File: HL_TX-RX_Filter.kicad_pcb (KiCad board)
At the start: 2 copper layers, 100 x 100 mm, 194 parts, among them J1 To Antenna, J10 CNR4, J2 From Tx, J3 ICSP, J4 Input1, J5 SCL SDA, J6 To Rx in, J7 CNR1, J8 CNR3, J9 CNR2, Q1 2N7002, Q2 2N7002, Q3 2N7002, Q4 2N7002, Q5 2N7002, Q6 2N7002, Q7 2N7002, Q8 2N7002, U1 LD1117S33TR, U10 PE4259, U11 PE4259, U12 PE4259, U13 PE4259, U2 ATMEGA328-AU, U3 PE4259, U4 PE4259, U5 PE4259, U6 PE4259, U7 PE4259, U8 PE4259, U9 PE4259

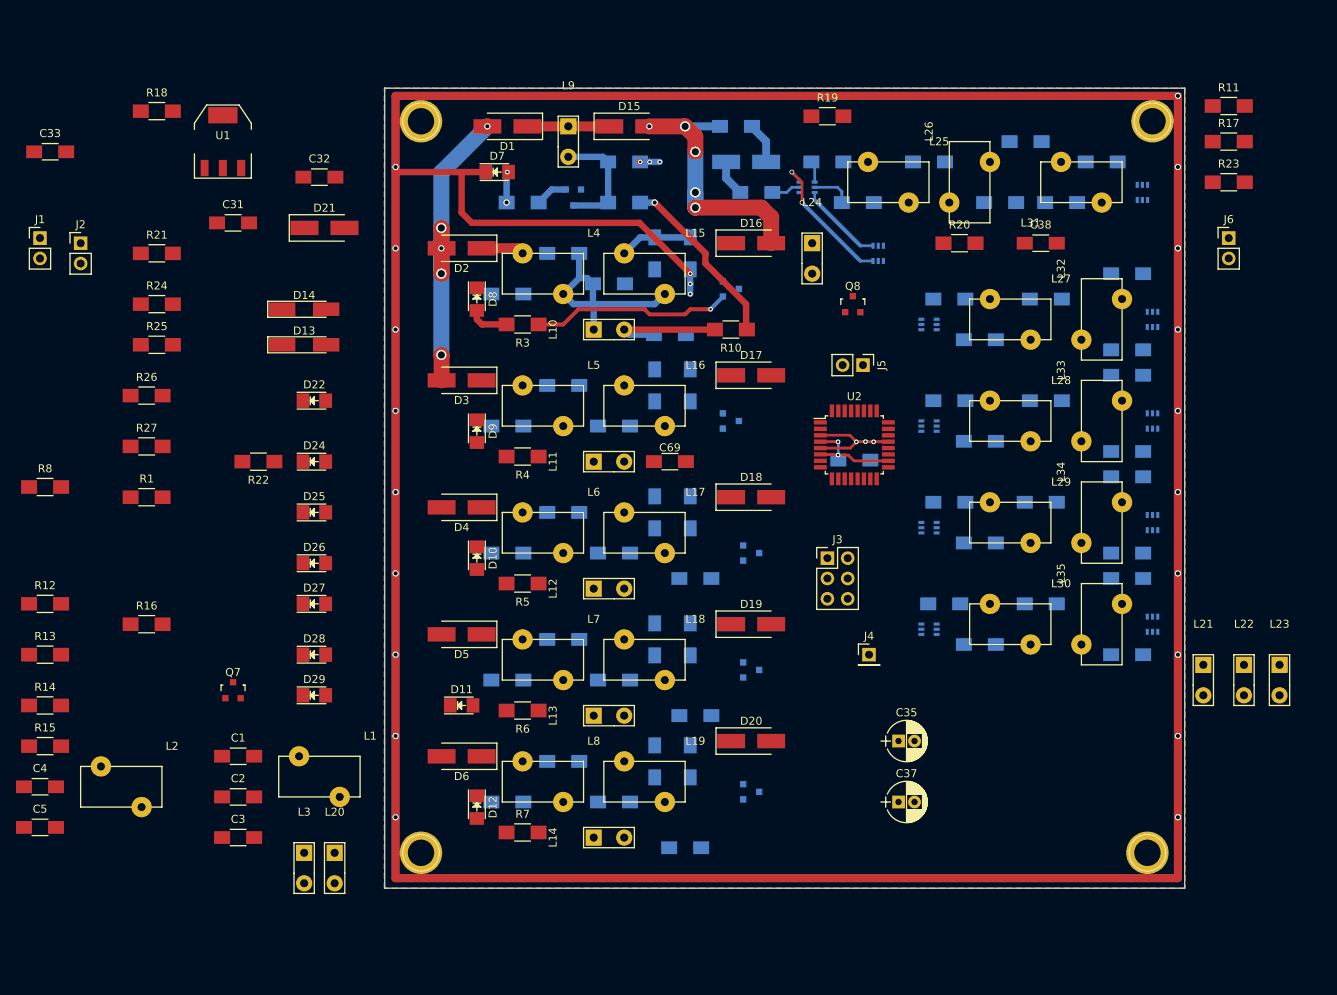
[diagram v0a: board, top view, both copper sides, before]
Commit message: Squeezed up Tx filters to hold 30M filter
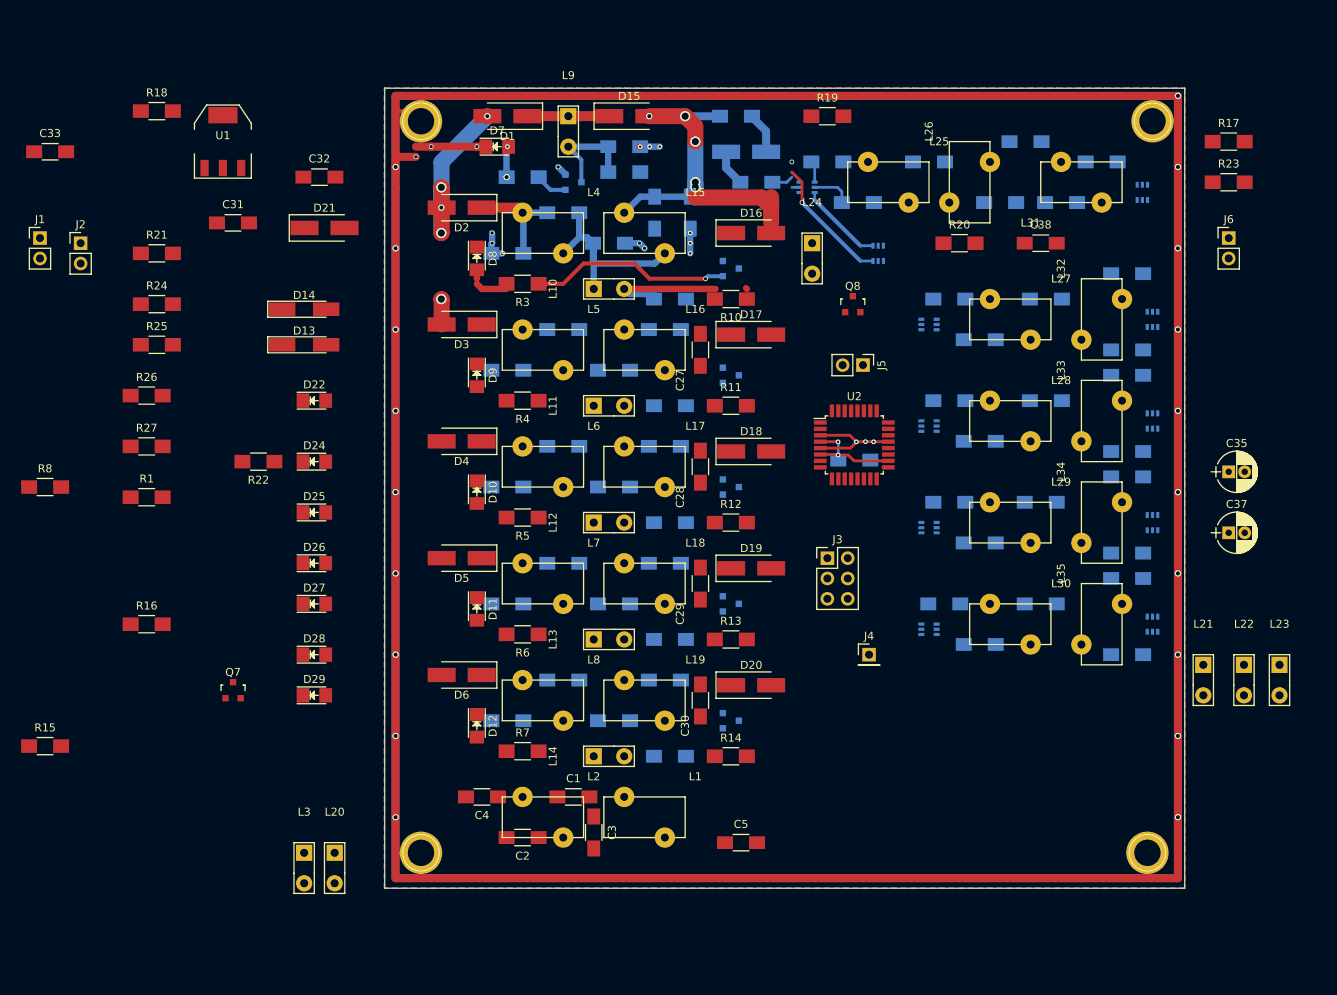
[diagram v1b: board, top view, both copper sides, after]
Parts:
- C27, C28, C29, C30: moved to F.Cu
- C69: moved to B.Cu
- moved C5 87.7 mm to (169.5, 154.3)
- moved R12 86.3 mm to (168.3, 114.3)
- moved R14 86.0 mm to (168.3, 143.5)
- moved R13 85.7 mm to (168.3, 128.9)
- moved R11 72.6 mm to (168.3, 99.7)
- moved C4 55.3 mm to (137.2, 148.6), turned to 180 degrees
- moved C37 53.3 mm to (230.5, 115.6)
- moved C35 53.3 mm to (230.5, 108.0)
- moved L2 52.8 mm to (139.7, 153.7)
- moved C3 44.5 mm to (151.1, 153.0), turned to 270 degrees
- moved C1 42.2 mm to (148.6, 148.6)
- moved L1 41.0 mm to (152.4, 153.7)
- moved C2 35.9 mm to (142.2, 153.7), turned to 180 degrees
- moved D11 12.2 mm to (136.5, 125.1), turned to 270 degrees
- moved C72 11.6 mm to (160.7, 143.5)
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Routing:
- net GND: track 859.2 -> 44.9 mm, vias 28 -> 17
- net (no net): track 0.00 -> 798.8 mm, vias 0 -> 21
- net Net-(C32-Pad1): track 34.6 -> 8.84 mm, vias 5 -> 1
- net Net-(C38-Pad1): track 22.5 -> 0.00 mm, vias 1 -> 0
- net Net-(C2-Pad1): track 43.8 -> 28.6 mm
- net Net-(C21-Pad2): track 9.08 -> 21.7 mm, vias 0 -> 4
- net Net-(C11-Pad1): track 5.38 -> 13.6 mm
- net Net-(C11-Pad2): track 27.4 -> 25.7 mm
- net Net-(C67-Pad1): track 14.9 -> 13.5 mm
- net 3V3: vias 4 -> 3

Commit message: Re-annotated board
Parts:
- removed U13: PE4259, TO_SOT_Packages_SMD:SC-70-6
- added R28: R, Resistors_SMD:R_1206_HandSoldering, F.Cu at (108.0, 121.9)
- added R29: R, Resistors_SMD:R_1206_HandSoldering, F.Cu at (101.0, 121.9)
- added R30: R, Resistors_SMD:R_1206_HandSoldering, F.Cu at (94.0, 121.9)
- added R31: R, Resistors_SMD:R_1206_HandSoldering, F.Cu at (108.0, 116.8)
- added R32: R, Resistors_SMD:R_1206_HandSoldering, F.Cu at (101.0, 116.8)
- added R33: R, Resistors_SMD:R_1206_HandSoldering, F.Cu at (94.0, 116.8)
- C1, C2, C3, C4, C5: moved to B.Cu
- C16: value 200p -> .1u
- C17: value 300p -> .1u
- C18: value 560p -> .1u
- C19: value 1082p -> .1u
- C20: value 2100p -> .1u
- C21: value 43p -> .1u
- C22: value 130p -> 300p
- C23: value 220p -> 560p
- C24: value 270p -> 1082p
- C25: value 552p -> 2100p
- C26: value 74p -> 200p
- C27: value 120p -> 43p
- C28: value 180p -> 130p
- C29: value 390p -> 220p
- C30: value 736p -> 270p
- C31: value 22p -> 552p
- C32: value C -> 74p
- C33: value 0.1u -> 120p
- C34: value 0.1 -> 180p
- C35: value 4.7u -> 390p; footprint Capacitors_THT:CP_Radial_D5.0mm_P2.00mm -> Capacitors_SMD:C_1206_HandSoldering
- C36: value C -> 736p
- C37: value 4.7u -> 22p; footprint Capacitors_THT:CP_Radial_D5.0mm_P2.00mm -> Capacitors_SMD:C_1206_HandSoldering
- C38: value 0.1u -> C
- C40: value 3000p -> 0.1
- C41: value 0.012u -> 4.7u; footprint Capacitors_SMD:C_1206_HandSoldering -> Capacitors_THT:CP_Radial_D5.0mm_P2.00mm
- C42: value 1600p -> C
- C43: value 1500p -> 4.7u; footprint Capacitors_SMD:C_1206_HandSoldering -> Capacitors_THT:CP_Radial_D5.0mm_P2.00mm
- C44: value 680p -> 0.1u
- C45: value 470p -> 0.1u
- C46: value 270p -> 3000p
- C47: value 2400p -> 0.012u
- C48: value 8200p -> 1600p
- C49: value 3900p -> 1500p
- C50: value 2400p -> 680p
- C51: value 1500p -> 470p
- C52: value 1800p -> 270p
- C53: value 680p -> 2400p
- C54: value 340p -> 8200p
- C55: value 236p -> 3900p
- C56: value 130p -> 2400p
- C57: value 3000p -> 1500p
- C58: value 2700p -> 1800p
- C59: value 1220p -> 680p
- C60: value 780p -> 340p
- C61: value 510p -> 236p
- C62: value 2400p -> 130p
- C63: value 2000p -> 3000p
- C64: value 1000p -> 2700p
- C65: value 680p -> 1220p
- C66: value 360p -> 780p
- C67: value .1u -> 510p
- C68: value .1u -> 2400p
- C69: value .1u -> 2000p
- C70: value .1u -> 1000p
- C71: value .1u -> 680p
- C72: value .1u -> 360p
- J1: value To Antenna -> CNR1; footprint Pin_Headers:Pin_Header_Straight_1x02_Pitch2.54mm -> Connectors:1pin
- J10: value CNR4 -> To Rx in; footprint Connectors:1pin -> Pin_Headers:Pin_Header_Straight_1x02_Pitch2.54mm
- J2: value From Tx -> CNR3; footprint Pin_Headers:Pin_Header_Straight_1x02_Pitch2.54mm -> Connectors:1pin
- J3: value ICSP -> CNR2; footprint Pin_Headers:Pin_Header_Straight_2x03_Pitch2.54mm -> Connectors:1pin
- J4: value Input1 -> CNR4; footprint Pin_Headers:Pin_Header_Straight_1x01_Pitch2.54mm -> Connectors:1pin
- J5: value SCL SDA -> To Antenna
- J6: value To Rx in -> From Tx
- J7: value CNR1 -> ICSP; footprint Connectors:1pin -> Pin_Headers:Pin_Header_Straight_2x03_Pitch2.54mm
- J8: value CNR3 -> SCL SDA; footprint Connectors:1pin -> Pin_Headers:Pin_Header_Straight_1x02_Pitch2.54mm
- J9: value CNR2 -> Input1; footprint Connectors:1pin -> Pin_Headers:Pin_Header_Straight_1x01_Pitch2.54mm
- R10, R9: value 100k -> R
- R11: value R -> 1k
- R12, R13: value R -> 100k
- R21: value 10k -> R
- R27: value R -> 10k
- R8: value 1k -> R
- U1: value LD1117S33TR -> ATMEGA328-AU; footprint TO_SOT_Packages_SMD:SOT-223 -> Housings_QFP:TQFP-32_7x7mm_Pitch0.8mm
- U10, U11, U12, U3, U4, U5, U6, U7, U8, U9: footprint TO_SOT_Packages_SMD:SC-70-6 -> TO_SOT_Packages_SMD:SOT-363_SC-70-6_Handsoldering
- U2: value ATMEGA328-AU -> PE4259; footprint Housings_QFP:TQFP-32_7x7mm_Pitch0.8mm -> TO_SOT_Packages_SMD:SOT-363_SC-70-6_Handsoldering
- moved L21 137.0 mm to (91.1, 146.1)
- moved L22 136.2 mm to (96.9, 145.4)
- moved L23 134.5 mm to (103.1, 146.3)
- moved J2 134.2 mm to (220.3, 64.1)
- moved R15 92.1 mm to (174.6, 141.0), turned to 270 degrees
- moved U1 87.5 mm to (183.5, 104.8)
- moved J8 81.7 mm to (194.9, 141.6)
- moved J7 78.1 mm to (185.4, 118.7)
- moved U2 66.1 mm to (175.0, 170.1)
- moved J4 60.4 mm to (130.2, 154.9)
- moved C41 60.3 mm to (184.8, 134.6)
- moved J9 59.5 mm to (83.8, 117.5)
- moved L20 57.6 mm to (175.9, 148.6)
- moved J5 57.1 mm to (170.2, 149.9), turned to 0 degrees
- moved J3 53.9 mm to (220.3, 154.9)
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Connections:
- C16 pad 1: Net-(C11-Pad2) -> Net-(C16-Pad1)
- C17 pad 1: Net-(C12-Pad2) -> Net-(C17-Pad1)
- C18 pad 1: Net-(C13-Pad2) -> Net-(C18-Pad1)
- C19 pad 1: Net-(C14-Pad2) -> Net-(C19-Pad1)
- C20 pad 1: Net-(C15-Pad2) -> Net-(C20-Pad1)
- C21 pad 1: Net-(C11-Pad2) -> Net-(C21-Pad1)
- C21 pad 2: Net-(C21-Pad2) -> GND
- C22 pad 2: Net-(C22-Pad2) -> GND
- C23 pad 2: Net-(C23-Pad2) -> GND
- C24 pad 2: Net-(C24-Pad2) -> GND
- C25 pad 2: Net-(C25-Pad2) -> GND
- C26 pad 1: Net-(C21-Pad2) -> Net-(C11-Pad2)
- C27 pad 1: Net-(C22-Pad2) -> Net-(C11-Pad2)
- C27 pad 2: GND -> Net-(C27-Pad2)
- C28 pad 1: Net-(C23-Pad2) -> Net-(C12-Pad2)
- C28 pad 2: GND -> Net-(C28-Pad2)
- C29 pad 1: Net-(C24-Pad2) -> Net-(C13-Pad2)
- C29 pad 2: GND -> Net-(C29-Pad2)
- C30 pad 1: Net-(C25-Pad2) -> Net-(C14-Pad2)
- C30 pad 2: GND -> Net-(C30-Pad2)
- C31 pad 1: Net-(C31-Pad1) -> Net-(C15-Pad2)
- C32 pad 1: Net-(C32-Pad1) -> Net-(C27-Pad2)
- C32 pad 2: Net-(C32-Pad2) -> GND
- C33 pad 1: Net-(C31-Pad2) -> Net-(C28-Pad2)
- C33 pad 2: Net-(C33-Pad2) -> GND
- C34 pad 1: 3V3 -> Net-(C29-Pad2)
- C35 pad 1: 3V3 -> Net-(C30-Pad2)
- C36 pad 1: Net-(C32-Pad1) -> Net-(C31-Pad2)
- C36 pad 2: Net-(C36-Pad2) -> GND
- C37 pad 1: 3V3 -> Net-(C37-Pad1)
- C37 pad 2: GND -> Net-(C37-Pad2)
- C38 pad 2: GND -> Net-(C38-Pad2)
- C39 pad 1: Net-(C39-Pad1) -> Net-(C37-Pad2)
- C40 pad 1: Net-(C40-Pad1) -> 3V3
- C40 pad 2: Net-(C40-Pad2) -> GND
- C41 pad 1: Net-(C41-Pad1) -> 3V3
- C42 pad 1: Net-(C40-Pad2) -> Net-(C38-Pad1)
- C43 pad 1: Net-(C43-Pad1) -> 3V3
- C43 pad 2: Net-(C43-Pad2) -> GND
- C44 pad 2: Net-(C44-Pad2) -> GND
- C48 pad 1: Net-(C48-Pad1) -> Net-(C46-Pad2)
- C48 pad 2: GND -> Net-(C48-Pad2)
- C49 pad 2: GND -> Net-(C49-Pad2)
- C50 pad 2: GND -> Net-(C50-Pad2)
- C51 pad 2: GND -> Net-(C51-Pad2)
- C52 pad 1: Net-(C42-Pad2) -> Net-(C52-Pad1)
- C53 pad 1: Net-(C43-Pad2) -> Net-(C53-Pad1)
- C53 pad 2: Net-(C53-Pad2) -> GND
- C54 pad 1: Net-(C44-Pad2) -> Net-(C54-Pad1)
- C54 pad 2: Net-(C54-Pad2) -> GND
- C55 pad 1: Net-(C45-Pad2) -> Net-(C55-Pad1)
- C55 pad 2: Net-(C55-Pad2) -> GND
- C56 pad 1: Net-(C46-Pad2) -> Net-(C56-Pad1)
- C56 pad 2: Net-(C56-Pad2) -> GND
- C58 pad 1: Net-(C58-Pad1) -> Net-(C48-Pad2)
- C58 pad 2: GND -> Net-(C58-Pad2)
- C59 pad 1: Net-(C59-Pad1) -> Net-(C49-Pad2)
- C59 pad 2: GND -> Net-(C59-Pad2)
- C60 pad 1: Net-(C60-Pad1) -> Net-(C50-Pad2)
- C60 pad 2: GND -> Net-(C60-Pad2)
- C61 pad 1: Net-(C61-Pad1) -> Net-(C51-Pad2)
- C61 pad 2: GND -> Net-(C61-Pad2)
- C63 pad 1: Net-(C53-Pad2) -> Net-(C63-Pad1)
- C63 pad 2: Net-(C63-Pad2) -> GND
- C64 pad 1: Net-(C54-Pad2) -> Net-(C64-Pad1)
- C64 pad 2: Net-(C64-Pad2) -> GND
- C65 pad 1: Net-(C55-Pad2) -> Net-(C65-Pad1)
- C65 pad 2: Net-(C65-Pad2) -> GND
- C66 pad 1: Net-(C56-Pad2) -> Net-(C66-Pad1)
- C66 pad 2: Net-(C66-Pad2) -> GND
- C68 pad 1: Net-(C68-Pad1) -> Net-(C58-Pad2)
- C68 pad 2: GND -> Net-(C68-Pad2)
- C69 pad 1: Net-(C69-Pad1) -> Net-(C59-Pad2)
- C69 pad 2: GND -> Net-(C69-Pad2)
- C70 pad 1: Net-(C70-Pad1) -> Net-(C60-Pad2)
- C70 pad 2: GND -> Net-(C70-Pad2)
- C71 pad 1: Net-(C71-Pad1) -> Net-(C61-Pad2)
- C71 pad 2: GND -> Net-(C71-Pad2)
- C72 pad 1: Net-(C72-Pad1) -> Net-(C62-Pad2)
- C72 pad 2: GND -> Net-(C72-Pad2)
- D13 pad 1: Net-(C31-Pad1) -> Net-(C37-Pad1)
- D14 pad 1: Net-(C38-Pad1) -> Net-(C44-Pad1)
- D14 pad 2: Net-(C31-Pad1) -> Net-(C37-Pad1)
- D15 pad 2: Net-(C32-Pad1) -> Net-(C38-Pad1)
- D16 pad 1: Net-(C21-Pad2) -> Net-(C27-Pad2)
- D16 pad 2: Net-(C32-Pad1) -> Net-(C38-Pad1)
- D17 pad 1: Net-(C22-Pad2) -> Net-(C28-Pad2)
- D17 pad 2: Net-(C32-Pad1) -> Net-(C38-Pad1)
- D18 pad 1: Net-(C23-Pad2) -> Net-(C29-Pad2)
- D18 pad 2: Net-(C32-Pad1) -> Net-(C38-Pad1)
- D19 pad 1: Net-(C24-Pad2) -> Net-(C30-Pad2)
- D19 pad 2: Net-(C32-Pad1) -> Net-(C38-Pad1)
- D20 pad 1: Net-(C25-Pad2) -> Net-(C31-Pad2)
- D20 pad 2: Net-(C32-Pad1) -> Net-(C38-Pad1)
- D21 pad 1: Net-(C31-Pad2) -> Net-(C37-Pad2)
- D21 pad 2: Net-(C32-Pad2) -> Net-(C38-Pad2)
- D23 pad 1: Net-(C39-Pad1) -> Net-(C45-Pad1)
- D23 pad 2: Net-(C36-Pad2) -> Net-(C42-Pad2)
- J1 pad 1: Net-(C1-Pad2) -> GND
- J10 pad 1: GND -> Net-(J10-Pad1)
- J2 pad 1: Net-(C33-Pad2) -> GND
- J3 pad 1: /I3 -> GND
- J4 pad 1: /I1 -> GND
- J5 pad 1: Net-(J5-Pad1) -> Net-(C1-Pad2)
- J5 pad 2: Net-(J5-Pad2) -> GND
- J6 pad 1: Net-(J6-Pad1) -> Net-(C39-Pad2)
- J7 pad 1: GND -> /I3
- J8 pad 1: GND -> Net-(J8-Pad1)
- J9 pad 1: GND -> /I1
- L10 pad 2: Net-(C68-Pad1) -> Net-(C17-Pad1)
- L11 pad 2: Net-(C69-Pad1) -> Net-(C18-Pad1)
- L12 pad 2: Net-(C70-Pad1) -> Net-(C19-Pad1)
- L13 pad 2: Net-(C71-Pad1) -> Net-(C20-Pad1)
- L14 pad 2: Net-(C72-Pad1) -> Net-(C21-Pad1)
- L15 pad 2: Net-(C21-Pad2) -> Net-(C27-Pad2)
- L16 pad 2: Net-(C22-Pad2) -> Net-(C28-Pad2)
- L17 pad 2: Net-(C23-Pad2) -> Net-(C29-Pad2)
- L18 pad 2: Net-(C24-Pad2) -> Net-(C30-Pad2)
- L19 pad 2: Net-(C25-Pad2) -> Net-(C31-Pad2)
- L20 pad 2: 3V3 -> Net-(L20-Pad2)
- L22 pad 1: Net-(C31-Pad2) -> Net-(C37-Pad2)
- L24 pad 1: Net-(C39-Pad1) -> Net-(C45-Pad1)
- L25 pad 1: Net-(C41-Pad1) -> Net-(C47-Pad1)
- L25 pad 2: Net-(C40-Pad2) -> Net-(C46-Pad2)
- L26 pad 1: Net-(C42-Pad2) -> Net-(C48-Pad2)
- L26 pad 2: Net-(C47-Pad1) -> Net-(C53-Pad1)
- L27 pad 1: Net-(C48-Pad1) -> Net-(C54-Pad1)
- L27 pad 2: Net-(C43-Pad2) -> Net-(C49-Pad2)
- L28 pad 1: Net-(C49-Pad1) -> Net-(C55-Pad1)
- L28 pad 2: Net-(C44-Pad2) -> Net-(C50-Pad2)
- L29 pad 1: Net-(C50-Pad1) -> Net-(C56-Pad1)
- L29 pad 2: Net-(C45-Pad2) -> Net-(C51-Pad2)
- L3 pad 2: 3V3 -> Net-(L20-Pad2)
- L30 pad 1: Net-(C51-Pad1) -> Net-(C57-Pad1)
- L30 pad 2: Net-(C46-Pad2) -> Net-(C52-Pad2)
- L31 pad 1: Net-(C52-Pad2) -> Net-(C58-Pad2)
- L31 pad 2: Net-(C57-Pad1) -> Net-(C63-Pad1)
- L32 pad 1: Net-(C53-Pad2) -> Net-(C59-Pad2)
- L32 pad 2: Net-(C58-Pad1) -> Net-(C64-Pad1)
- L33 pad 1: Net-(C54-Pad2) -> Net-(C60-Pad2)
- L33 pad 2: Net-(C59-Pad1) -> Net-(C65-Pad1)
- L34 pad 1: Net-(C55-Pad2) -> Net-(C61-Pad2)
- L34 pad 2: Net-(C60-Pad1) -> Net-(C66-Pad1)
- L35 pad 1: Net-(C56-Pad2) -> Net-(C62-Pad2)
- L35 pad 2: Net-(C61-Pad1) -> Net-(C67-Pad1)
- L9 pad 2: Net-(C67-Pad1) -> Net-(C16-Pad1)
- Q1 pad 3: Net-(C67-Pad1) -> Net-(C16-Pad1)
- Q2 pad 3: Net-(C68-Pad1) -> Net-(C17-Pad1)
- Q3 pad 3: Net-(C69-Pad1) -> Net-(C18-Pad1)
- Q4 pad 3: Net-(C70-Pad1) -> Net-(C19-Pad1)
- Q5 pad 3: Net-(C71-Pad1) -> Net-(C20-Pad1)
- Q6 pad 3: Net-(C72-Pad1) -> Net-(C21-Pad1)
- R10 pad 1: Net-(C38-Pad1) -> /T160
- R10 pad 2: Net-(C68-Pad1) -> Net-(D12-Pad2)
- R11 pad 1: Net-(C38-Pad1) -> Net-(D13-Pad2)
- R11 pad 2: Net-(C69-Pad1) -> (no net)
- R12 pad 1: Net-(C38-Pad1) -> Net-(C44-Pad1)
- R12 pad 2: Net-(C70-Pad1) -> Net-(C16-Pad1)
- R13 pad 1: Net-(C38-Pad1) -> Net-(C44-Pad1)
- R13 pad 2: Net-(C71-Pad1) -> Net-(C17-Pad1)
- R14 pad 1: Net-(C38-Pad1) -> Net-(C44-Pad1)
- R14 pad 2: Net-(C72-Pad1) -> Net-(C18-Pad1)
- R15 pad 1: Net-(C32-Pad1) -> Net-(C44-Pad1)
- R15 pad 2: Net-(L20-Pad1) -> Net-(C19-Pad1)
- R16 pad 1: Net-(C32-Pad2) -> Net-(C44-Pad1)
- R16 pad 2: Net-(L21-Pad2) -> Net-(C20-Pad1)
- R17 pad 1: Net-(L22-Pad2) -> Net-(C44-Pad1)
- R17 pad 2: Net-(C38-Pad1) -> Net-(C21-Pad1)
- R18 pad 1: /Tptt -> Net-(C38-Pad1)
- R18 pad 2: Net-(D22-Pad2) -> Net-(L20-Pad1)
- R19 pad 1: Net-(L23-Pad1) -> Net-(C38-Pad1)
- R19 pad 2: Net-(C36-Pad2) -> Net-(L20-Pad1)
- R2 pad 1: /T0 -> Net-(C2-Pad1)
- R2 pad 2: Net-(D7-Pad2) -> Net-(L3-Pad1)
- R20 pad 1: Net-(L24-Pad2) -> Net-(C38-Pad1)
- R20 pad 2: Net-(C38-Pad1) -> Net-(L20-Pad1)
- R21 pad 1: 3V3 -> Net-(C38-Pad1)
- R21 pad 2: /RESET -> Net-(L20-Pad1)
- R22 pad 1: /R1 -> Net-(C38-Pad2)
- R22 pad 2: Net-(D24-Pad2) -> Net-(L21-Pad2)
- R23 pad 1: /R2 -> Net-(L22-Pad2)
- R23 pad 2: Net-(D25-Pad2) -> Net-(C44-Pad1)
- R24 pad 1: /R3 -> /Tptt
- R24 pad 2: Net-(D26-Pad2) -> Net-(D22-Pad2)
- R25 pad 1: /R4 -> Net-(L23-Pad1)
- R25 pad 2: Net-(D27-Pad2) -> Net-(C42-Pad2)
- R26 pad 1: /R5 -> Net-(L24-Pad2)
- R26 pad 2: Net-(D28-Pad2) -> Net-(C44-Pad1)
- R27 pad 1: /R0 -> 3V3
- R27 pad 2: Net-(D29-Pad2) -> /RESET
- R3 pad 1: /T17 -> Net-(C2-Pad1)
- R3 pad 2: Net-(D8-Pad2) -> Net-(L3-Pad1)
- R4 pad 1: /T30 -> Net-(C2-Pad1)
- R4 pad 2: Net-(D9-Pad2) -> Net-(L3-Pad1)
- R5 pad 1: /T40 -> /T0
- R5 pad 2: Net-(D10-Pad2) -> Net-(D7-Pad2)
- R6 pad 1: /T80 -> /T17
- R6 pad 2: Net-(D11-Pad2) -> Net-(D8-Pad2)
- R7 pad 1: /T160 -> /T30
- R7 pad 2: Net-(D12-Pad2) -> Net-(D9-Pad2)
- R8 pad 1: Net-(D13-Pad2) -> /T40
- R8 pad 2: +12V -> Net-(D10-Pad2)
- R9 pad 1: Net-(C38-Pad1) -> /T80
- R9 pad 2: Net-(C67-Pad1) -> Net-(D11-Pad2)
- U1 pad 1: GND -> /T17
- U1 pad 2: 3V3 -> /T30
- U1 pad 3: +12V -> GND
- U1 pad 4: (no net) -> 3V3
- U10 pad 1: Net-(C63-Pad2) -> Net-(C70-Pad2)
- U10 pad 3: Net-(U10-Pad3) -> (no net)
- U10 pad 4: /R2 -> /R3
- U11 pad 1: Net-(C64-Pad2) -> Net-(C71-Pad2)
- U11 pad 3: Net-(U11-Pad3) -> (no net)
- U11 pad 4: /R3 -> /R4
- U12 pad 1: Net-(C65-Pad2) -> Net-(C72-Pad2)
- U12 pad 3: Net-(U12-Pad3) -> (no net)
- U12 pad 4: /R4 -> /R5
- U2 pad 1: /T17 -> Net-(C46-Pad1)
- U2 pad 2: /T30 -> GND
- U2 pad 3: GND -> Net-(U2-Pad3)
- U2 pad 4: 3V3 -> /R1
- U2 pad 5: GND -> Net-(C45-Pad2)
- U3 pad 1: Net-(C40-Pad1) -> Net-(U2-Pad3)
- U3 pad 3: Net-(U3-Pad3) -> (no net)
- U3 pad 4: /R1 -> /R0
- U3 pad 5: Net-(C39-Pad2) -> Net-(J10-Pad1)
- U4 pad 1: Net-(U3-Pad3) -> Net-(C49-Pad1)
- U4 pad 3: Net-(U4-Pad3) -> (no net)
- U4 pad 4: /R0 -> /R2
- U4 pad 5: Net-(J6-Pad1) -> Net-(J10-Pad1)
- U5 pad 1: Net-(C43-Pad1) -> Net-(C50-Pad1)
- U5 pad 3: Net-(U5-Pad3) -> (no net)
- U5 pad 4: /R2 -> /R3
- U5 pad 5: Net-(J6-Pad1) -> Net-(J10-Pad1)
- U6 pad 1: Net-(C44-Pad1) -> Net-(C51-Pad1)
- U6 pad 3: Net-(U6-Pad3) -> (no net)
- U6 pad 4: /R3 -> /R4
- U6 pad 5: Net-(J6-Pad1) -> Net-(J10-Pad1)
- U7 pad 1: Net-(C45-Pad1) -> Net-(C52-Pad1)
- U7 pad 3: Net-(U7-Pad3) -> (no net)
- U7 pad 4: /R4 -> /R5
- U7 pad 5: Net-(J6-Pad1) -> Net-(J10-Pad1)
- U8 pad 1: Net-(C46-Pad1) -> Net-(C68-Pad2)
- U8 pad 3: Net-(U8-Pad3) -> (no net)
- U8 pad 4: /R5 -> /R1
- U8 pad 5: Net-(J6-Pad1) -> Net-(U10-Pad5)
- U9 pad 1: Net-(C62-Pad2) -> Net-(C69-Pad2)
- U9 pad 3: Net-(U9-Pad3) -> (no net)
- U9 pad 4: /R1 -> /R2
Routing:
- net (no net): track 798.8 -> 0.06 mm, vias 21 -> 0
- net GND: track 44.9 -> 813.9 mm, vias 17 -> 33
- net 3V3: track 31.9 -> 0.58 mm, vias 3 -> 0
- net Net-(C1-Pad1): track 0.00 -> 26.4 mm
- net /T17: track 25.0 -> 0.00 mm, vias 1 -> 0
- net Net-(C21-Pad2): track 21.7 -> 0.00 mm, vias 4 -> 0
- net Net-(C11-Pad2): track 25.7 -> 5.91 mm
- net Net-(C68-Pad1): track 15.4 -> 0.00 mm
- net Net-(C67-Pad1): track 13.5 -> 0.00 mm
- net Net-(C2-Pad1): track 28.6 -> 16.1 mm, vias 5 -> 2
- net Net-(C1-Pad2): track 0.00 -> 12.4 mm
- net Net-(U3-Pad3): track 10.6 -> 0.00 mm
- net Net-(C32-Pad1): track 8.84 -> 0.00 mm, vias 1 -> 0
- net Net-(C16-Pad1): track 0.00 -> 6.15 mm
- net Net-(C36-Pad2): track 5.18 -> 0.00 mm
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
